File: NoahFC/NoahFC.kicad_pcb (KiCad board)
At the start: 2 copper layers, 40 x 45 mm, 25 parts, among them J1 CH1, J10 GND, J2 CH2, J3 MPU6050, J4 FTDI, J5 8.4V, J6 CH3, J7 PPM, J8 GPS, J9 CH4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

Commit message: revision 1
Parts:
- added J11: SCK, TestPoint:TestPoint_Pad_1.0x1.0mm, F.Cu at (150.8, 88.0)
- added J12: MISO, TestPoint:TestPoint_Pad_1.0x1.0mm, F.Cu at (150.8, 85.4)
- added J13: VCC, TestPoint:TestPoint_Pad_4.0x4.0mm, F.Cu at (159.4, 98.7)
- added J14: GND, TestPoint:TestPoint_Pad_4.0x4.0mm, F.Cu at (154.0, 98.7)
- added R5: 100K, Resistor_SMD:R_0805_2012Metric, F.Cu at (139.4, 90.9)
- added R6: 10K, Resistor_SMD:R_0805_2012Metric, F.Cu at (134.9, 90.9)
- C3: value 100nF -> 1nF
- C5: value 100uF -> 10uF
- D1, D2, D3: footprint LED_SMD:LED_0603_1608Metric -> LED_SMD:LED_0805_2012Metric
- J5: value 8.4V -> VCC
- U1: value ATmega328-A -> ATmega328
- moved C5 36.1 mm to (134.8, 94.1)
- moved J10 34.2 mm to (134.6, 98.7)
- moved C3 34.1 mm to (134.0, 73.2), turned to 180 degrees
- moved J5 29.3 mm to (140.0, 98.7)
- moved R1 23.4 mm to (138.5, 76.9), turned to -90 degrees
- moved C4 22.9 mm to (139.4, 94.1), turned to 0 degrees
- moved U3 21.9 mm to (145.6, 91.0), turned to 90 degrees
- moved J8 18.4 mm to (152.5, 92.7)
- moved J9 17.7 mm to (155.0, 77.5), turned to 90 degrees
- moved J6 14.6 mm to (155.0, 80.1), turned to 90 degrees
- moved D2 13.2 mm to (160.0, 62.2), turned to 0 degrees
- moved R3 13.1 mm to (160.0, 59.3), turned to 0 degrees
- moved J2 11.8 mm to (155.0, 82.7), turned to 90 degrees
- moved D3 11.7 mm to (160.0, 72.4), turned to 0 degrees
- moved D1 11.2 mm to (160.0, 67.3), turned to 0 degrees
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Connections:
- net Net-(C1-Pad1) renamed XTAL1
- net Net-(C2-Pad1) renamed XTAL2
- net Net-(U1-Pad2) renamed LED_MODE
- C3 pad 1: 5V -> RESET
- J1 pad 2: 5V -> 5V_BEC
- J2 pad 2: 5V -> 5V_BEC
- J6 pad 2: unconnected-(J6-Pad2) -> 5V_BEC
- J7 pad 2: 5V -> 5V_BEC
- J9 pad 2: 5V -> 5V_BEC
- R1 pad 1: Net-(R1-Pad1) -> RESET
- R2 pad 1: Net-(U1-Pad32) -> LED_GPS
- R4 pad 1: Net-(U1-Pad9) -> LED_PWR
- U1 pad 11: GPS_RX -> LED_PWR
- U1 pad 16: unconnected-(U1-Pad16) -> MISO
- U1 pad 17: unconnected-(U1-Pad17) -> SCK
- U1 pad 19: unconnected-(U1-Pad19) -> ADC6
- U1 pad 22: unconnected-(U1-Pad22) -> ADC7
- U1 pad 23: unconnected-(U1-Pad23) -> A0
- U1 pad 24: unconnected-(U1-Pad24) -> A1
- U1 pad 25: unconnected-(U1-Pad25) -> VOLTAGE_READ
- U1 pad 26: unconnected-(U1-Pad26) -> A3
- U1 pad 29: Net-(R1-Pad1) -> RESET
- U1 pad 32: Net-(U1-Pad32) -> GPS_RX
- U1 pad 9: Net-(U1-Pad9) -> LED_GPS
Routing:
- net 5V: track 166.3 -> 0.00 mm, vias 10 -> 0
- net GND: track 157.1 -> 0.00 mm
- net DTR: track 44.0 -> 0.00 mm, vias 2 -> 0
- net Net-(U1-Pad32): track 33.9 -> 0.00 mm, vias 2 -> 0
- net Net-(U1-Pad9): track 33.9 -> 0.00 mm, vias 2 -> 0
- net RX: track 24.4 -> 0.00 mm, vias 2 -> 0
- net TX: track 23.9 -> 0.00 mm
- net LED_MODE: track 22.9 -> 0.00 mm, vias 2 -> 0
- net GPS_RX: track 22.8 -> 0.00 mm
- net GPS_TX: track 21.2 -> 0.00 mm
- net SCL: track 19.1 -> 0.00 mm
- net SDA: track 19.0 -> 0.00 mm, vias 2 -> 0
- net PPM: track 18.8 -> 0.00 mm, vias 2 -> 0
- net CH4: track 15.3 -> 0.00 mm, vias 2 -> 0
- net XTAL1: track 14.0 -> 0.00 mm
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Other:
- board size 40 x 45 mm -> 30 x 43 mm
- board text added: "- 8.4v +"
- board text added: "- ESC +"
- board text added: "NoahFC rev1"
- board text added: "http://github.com/zosko/NoahFC by Bosko"
- board text removed: "G"
- board text removed: "NoahFC rev0"
- board text removed: "S"

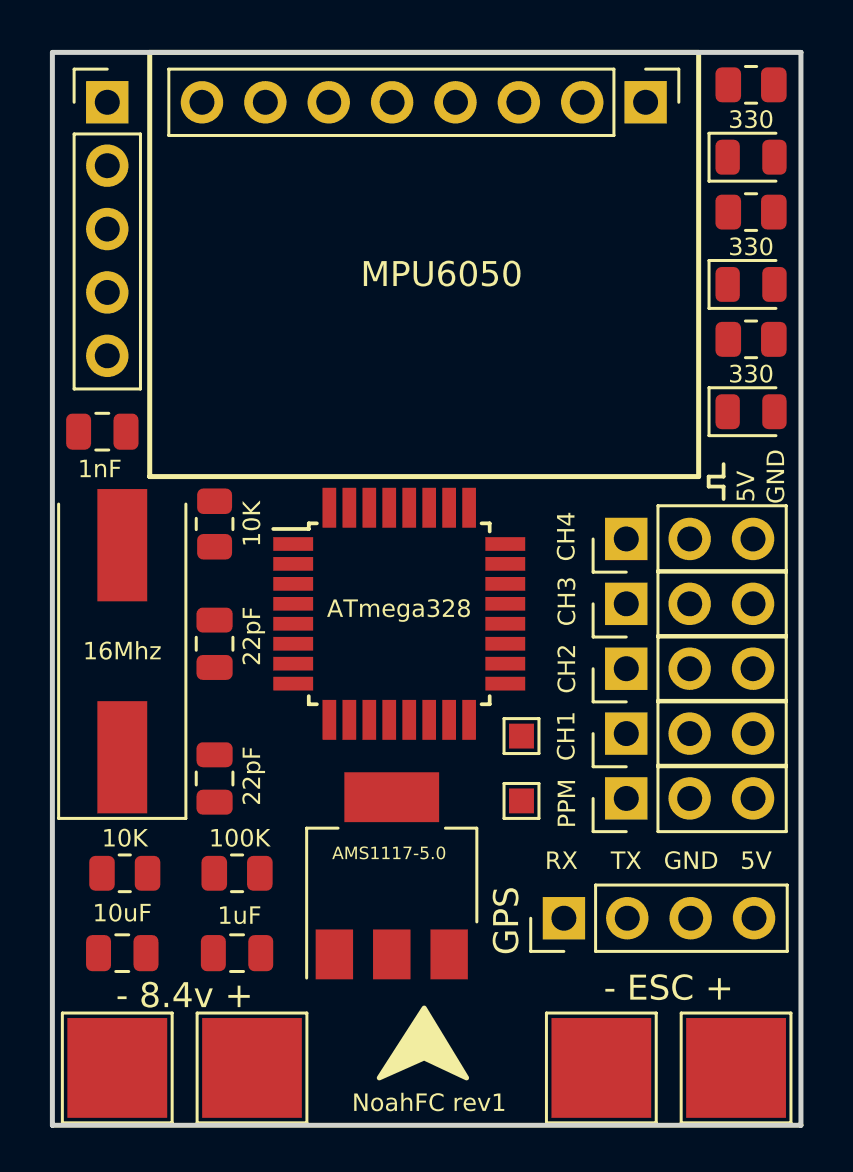
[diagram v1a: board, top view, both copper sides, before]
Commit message: remove one aleron servo
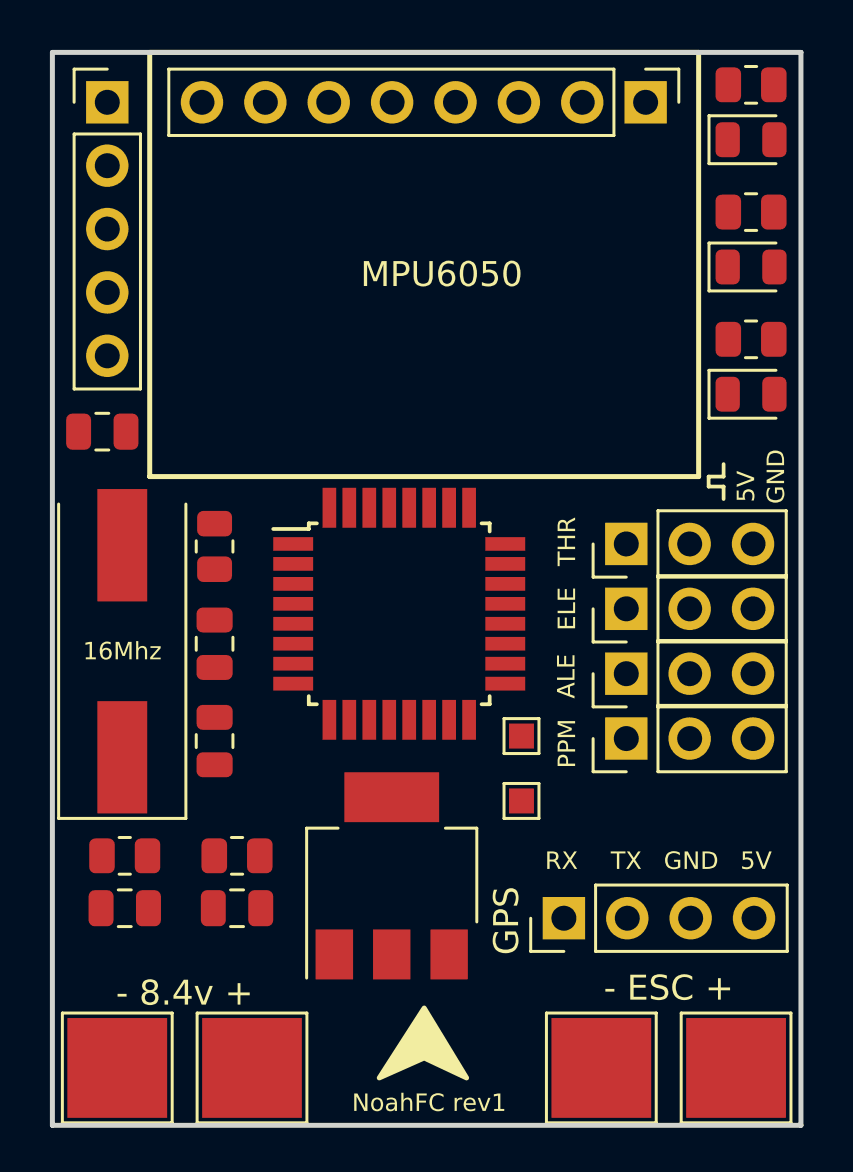
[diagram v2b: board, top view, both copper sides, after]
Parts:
- removed J9: CH4, Connector_PinHeader_2.54mm:PinHeader_1x03_P2.54mm_Vertical
- D1: value PWR -> GPS
- D2: value GPS -> MODE
- D3: value MODE -> PWR
- J1: value CH1 -> ALE
- J2: value CH2 -> ELE
- J6: value CH3 -> THR
- moved J2 2.40 mm to (155.0, 80.3)
- moved J7 2.40 mm to (155.0, 85.5)
- moved J1 2.40 mm to (155.0, 82.9)
- moved J6 2.40 mm to (155.0, 77.7)
- moved C5 1.80 mm to (134.9, 92.3)
- moved C4 1.80 mm to (139.4, 92.3)
- moved C2 1.50 mm to (138.5, 85.6)
- moved R1 0.90 mm to (138.5, 77.8)
- moved D1 0.70 mm to (160.0, 66.6)
- moved D2 0.70 mm to (160.0, 61.5)
- moved D3 0.70 mm to (160.0, 71.7)
- moved R5 0.70 mm to (139.4, 90.2)
- moved R6 0.70 mm to (134.9, 90.2)
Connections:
- net CH1 renamed ALERON
- net CH2 renamed ELEVATOR
- net CH3 renamed THROTTLE
- U1 pad 10: CH4 -> D6

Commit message: route board
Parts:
- added J15: A1, TestPoint:TestPoint_Pad_1.0x1.0mm, F.Cu at (154.5, 76.2)
- added J16: A3, TestPoint:TestPoint_Pad_1.0x1.0mm, F.Cu at (152.4, 76.2)
- added J17: D6, TestPoint:TestPoint_Pad_1.0x1.0mm, F.Cu at (140.9, 87.6)
- added J9: A0, TestPoint:TestPoint_Pad_1.0x1.0mm, F.Cu at (156.7, 76.2)
- moved J2 1.60 mm to (155.0, 81.9)
- moved J1 1.60 mm to (155.0, 84.5)
- moved J6 1.60 mm to (155.0, 79.3)
- moved J7 1.60 mm to (155.0, 87.1)
- moved J12 1.17 mm to (151.4, 86.4)
- moved J11 0.92 mm to (151.4, 88.7)
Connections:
- J1 pad 3: GND -> GND_BEC
- J2 pad 3: GND -> GND_BEC
- J6 pad 3: GND -> GND_BEC
- J7 pad 3: GND -> GND_BEC
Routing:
- net GND: track 0.00 -> 135.7 mm, vias 0 -> 7
- net 5V: track 0.00 -> 120.4 mm, vias 0 -> 7
- net LED_GPS: track 0.00 -> 68.2 mm, vias 0 -> 10
- net VOLTAGE_READ: track 0.00 -> 56.5 mm, vias 0 -> 2
- net LED_MODE: track 0.00 -> 44.0 mm, vias 0 -> 4
- net GPS_RX: track 0.00 -> 41.4 mm, vias 0 -> 1
- net PPM: track 0.00 -> 39.4 mm, vias 0 -> 2
- net VCC: track 0.00 -> 36.0 mm, vias 0 -> 4
- net RESET: track 0.00 -> 27.1 mm, vias 0 -> 2
- net SDA: track 0.00 -> 25.7 mm
- net LED_PWR: track 0.00 -> 23.1 mm, vias 0 -> 2
- net TX: track 0.00 -> 21.4 mm
- net RX: track 0.00 -> 21.0 mm, vias 0 -> 2
- net GPS_TX: track 0.00 -> 20.9 mm, vias 0 -> 1
- net SCL: track 0.00 -> 20.4 mm
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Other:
- board text added: "- VCC +"
- board text removed: "- 8.4v +"

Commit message: rev1 updates
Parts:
- moved J14 5.50 mm to (159.5, 98.6)
- moved J13 4.90 mm to (154.5, 98.6)
- moved J5 0.61 mm to (139.4, 98.6)
- moved J10 0.22 mm to (134.4, 98.6)
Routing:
- net GND: track 135.7 -> 142.8 mm, vias 7 -> 55
- net VCC: track 36.0 -> 32.5 mm, vias 4 -> 2
- net 5V: track 120.4 -> 117.2 mm, vias 7 -> 5
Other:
- board text added: "+ ESC -"
- board text removed: "- ESC +"

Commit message: pin improve
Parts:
- turned R5 to 180 degrees
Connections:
- J7 pad 2: 5V_BEC -> 5V
- J7 pad 3: GND_BEC -> GND
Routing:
- net 5V: track 117.2 -> 124.9 mm
- net GND: track 142.8 -> 150.4 mm
- net VOLTAGE_READ: track 56.5 -> 51.8 mm
- net GND_BEC: track 7.80 -> 5.20 mm
- net 5V_BEC: track 7.80 -> 5.20 mm
- net VCC: track 32.5 -> 31.8 mm

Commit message: fill board
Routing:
- net 5V: track 124.9 -> 127.1 mm
- net PPM: track 39.4 -> 40.9 mm
- net LED_GPS: track 68.2 -> 68.9 mm
- added copper zone on B.Cu, net GND
- added copper zone on F.Cu, net GND

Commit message: add RESET pad
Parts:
- added J18: RESET, TestPoint:TestPoint_Pad_1.0x1.0mm, F.Cu at (138.3, 72.3)
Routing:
- net RESET: track 27.1 -> 29.0 mm
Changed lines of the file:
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@@
       (net 2 "VCC") (pinfunction "Pin_1") (pintype "passive"))
+  )
+  (footprint "TestPoint:TestPoint_Pad_1.0x1.0mm" (layer "F.Cu")
+    (at 138.3 72.3)
+    (descr "SMD rectangular pad as test Point, square 1.0mm side length")
+    (tags "test point SMD pad rectangle square")
+    (property "Sheetfile" "NoahFC.kicad_sch")
+    (property "Sheetname" "")
+    (attr exclude_from_pos_files)
+    (fp_text reference "J18" (at 0 -1.448) (layer "F.SilkS") hide
+      (effects (font (size 1 1) (thickness 0.15)))
+    )
+    (fp_text value "RESET" (at 0 1.55) (layer "F.Fab") hide
+      (effects (font (size 1 1) (thickness 0.15)))
+    )
+    (fp_text user "${REFERENCE}" (at 0 -1.45) (layer "F.Fab") hide
+      (effects (font (size 1 1) (thickness 0.15)))
+    )
+    (fp_line (start -0.7 0.7) (end -0.7 -0.7) (layer "F.SilkS") (width 0.12))
+    (fp_line (start -0.7 -0.7) (end 0.7 -0.7) (layer "F.SilkS") (width 0.12))
+    (fp_line (start 0.7 -0.7) (end 0.7 0.7) (layer "F.SilkS") (width 0.12))
+    (fp_line (start 0.7 0.7) (end -0.7 0.7) (layer "F.SilkS") (width 0.12))
+    (fp_line (start -1 -1) (end 1 -1) (layer "F.CrtYd") (width 0.05))
+    (fp_line (start 1 1) (end -1 1) (layer "F.CrtYd") (width 0.05))
+    (fp_line (start 1 1) (end 1 -1) (layer "F.CrtYd") (width 0.05))
+    (fp_line (start -1 -1) (end -1 1) (layer "F.CrtYd") (width 0.05))
+    (pad "1" smd rect (at 0 0) (size 1 1) (layers "F.Cu" "F.Mask")
+      (net 24 "RESET") (pinfunction "Pin_1") (pintype "passive"))
   )
   (footprint "TestPoint:TestPoint_Pad_4.0x4.0mm" (layer "F.Cu")
@@
   (segment (start 143 75.1) (end 138.5 75.1) (width 0.25) (layer "B.Cu") (net 23))
   (segment (start 138.5 75.1) (end 134.4 79.2) (width 0.25) (layer "B.Cu") (net 23))
+  (segment (start 136.725 71.425) (end 134.95 73.2) (width 0.25) (layer "F.Cu") (net 24))
+  (segment (start 138.3 72.3) (end 137.6 72.3) (width 0.25) (layer "F.Cu") (net 24))
   (segment (start 143.1755 67.3) (end 140.85 67.3) (width 0.25) (layer "F.Cu") (net 24))
+  (segment (start 140.85 67.3) (end 136.725 71.425) (width 0.25) (layer "F.Cu") (net 24))
   (segment (start 145.5 76.25) (end 145.5 67.3) (width 0.25) (layer "F.Cu") (net 24))
+  (segment (start 137.6 72.3) (end 136.725 71.425) (width 0.25) (layer "F.Cu") (net 24))
   (segment (start 134.95 73.3375) (end 138.5 76.8875) (width 0.25) (layer "F.Cu") (net 24))
-  (segment (start 140.85 67.3) (end 134.95 73.2) (width 0.25) (layer "F.Cu") (net 24))
   (segment (start 134.95 73.2) (end 134.95 73.3375) (width 0.25) (layer "F.Cu") (net 24))
   (via (at 145.5 67.3) (size 0.8) (drill 0.4) (layers "F.Cu" "B.Cu") (net 24))

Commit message: add rev2 version board
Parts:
- removed J15: A1, TestPoint:TestPoint_Pad_1.0x1.0mm
- removed J3: MPU6050, Connector_PinHeader_2.54mm:PinHeader_1x08_P2.54mm_Vertical
- removed J9: A0, TestPoint:TestPoint_Pad_1.0x1.0mm
- added C10: 10uF, Capacitor_SMD:C_0805_2012Metric, F.Cu at (143.6, 108.9)
- added C11: 22uF, Capacitor_SMD:C_0805_2012Metric, F.Cu at (139.7, 108.9)
- added C12: 22pF, Capacitor_SMD:C_0805_2012Metric, F.Cu at (120.1, 105.6)
- added C13: 22pF, Capacitor_SMD:C_0805_2012Metric, F.Cu at (120.1, 103.4)
- added C17: 100nF, Capacitor_SMD:C_0805_2012Metric, F.Cu at (140.0, 104.3)
- added C18: 47uF, Capacitor_Tantalum_SMD:CP_EIA-3216-18_Kemet-A, F.Cu at (134.5, 108.8)
- added C19: 47uF, Capacitor_Tantalum_SMD:CP_EIA-3216-18_Kemet-A, F.Cu at (128.8, 108.8)
- added C20: 4.7uF, Capacitor_SMD:C_0805_2012Metric, F.Cu at (144.4, 78.6)
- added C21: 220nF, Capacitor_SMD:C_0805_2012Metric, F.Cu at (142.0, 78.6)
- added C6: 10nF, Capacitor_SMD:C_0805_2012Metric, F.Cu at (126.2, 88.1)
- added C7: 100nF, Capacitor_SMD:C_0805_2012Metric, F.Cu at (128.3, 82.2)
- added C8: 100nF, Capacitor_SMD:C_0805_2012Metric, F.Cu at (123.2, 87.4)
- added C9: 2200pF, Capacitor_SMD:C_0805_2012Metric, F.Cu at (124.4, 76.7)
- added R10: 75, Resistor_SMD:R_0805_2012Metric, F.Cu at (140.0, 102.2)
- added R7: 10K, Resistor_SMD:R_0805_2012Metric, F.Cu at (132.0, 76.8)
- added R8: 10K, Resistor_SMD:R_0805_2012Metric, F.Cu at (132.0, 80.3)
- added R9: 75, Resistor_SMD:R_0805_2012Metric, F.Cu at (140.0, 106.4)
- added U2: MPU-6050, Sensor_Motion:InvenSense_QFN-24_4x4mm_P0.5mm, F.Cu at (122.9, 81.9)
- added U4: AMS1117-3.3, Package_TO_SOT_SMD:SOT-223-3_TabPin2, F.Cu at (141.6, 114.4)
- added U5: MAX7456EUI+, MAX7456:SOP65P637X110-28N, F.Cu at (131.7, 114.9)
- added U6: HMC5883L, HMC5883L:LPCC-16, F.Cu at (137.7, 78.5)
- added Y2: 27Mhz, Crystal:Crystal_SMD_3225-4Pin_3.2x2.5mm, F.Cu at (116.4, 104.5)
- J16: value A3 -> CAM; footprint TestPoint:TestPoint_Pad_1.0x1.0mm -> Connector_PinHeader_2.54mm:PinHeader_1x02_P2.54mm_Vertical
- J17: value D6 -> VTX; footprint TestPoint:TestPoint_Pad_1.0x1.0mm -> Connector_PinHeader_2.54mm:PinHeader_1x02_P2.54mm_Vertical
- Y1: footprint Crystal:Crystal_SMD_HC49-SD -> Crystal:Crystal_SMD_3225-4Pin_3.2x2.5mm
- moved R4 59.9 mm to (133.5, 123.2), turned to 180 degrees
- moved D3 59.6 mm to (130.0, 123.2)
- moved J14 49.4 mm to (116.5, 122.9)
- moved J13 40.9 mm to (121.6, 122.9)
- moved U3 33.0 mm to (122.2, 114.3)
- moved R5 32.3 mm to (130.0, 121.1), turned to 0 degrees
- moved R3 31.2 mm to (131.1, 71.1)
- moved R6 30.9 mm to (133.5, 121.1), turned to 0 degrees
- moved J16 30.1 mm to (147.9, 106.0), turned to -90 degrees
- moved J12 28.8 mm to (129.7, 105.4)
- moved J10 27.5 mm to (147.3, 122.9)
- moved D2 27.2 mm to (134.6, 71.1)
- moved Y1 25.7 mm to (116.4, 100.0)
- moved C1 25.2 mm to (120.1, 98.9), turned to 0 degrees
- moved J11 24.6 mm to (133.4, 105.5)
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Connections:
- J16 pad 1: A3 -> GND
- J17 pad 1: D6 -> GND
- R4 pad 1: LED_PWR -> 5V
- U1 pad 10: D6 -> ELEVATOR
- U1 pad 11: LED_PWR -> LED_GPS
- U1 pad 14: ELEVATOR -> SS
- U1 pad 15: THROTTLE -> MOSI
- U1 pad 19: ADC6 -> unconnected-(U1-Pad19)
- U1 pad 22: ADC7 -> unconnected-(U1-Pad22)
- U1 pad 23: A0 -> unconnected-(U1-Pad23)
- U1 pad 24: A1 -> unconnected-(U1-Pad24)
- U1 pad 26: A3 -> unconnected-(U1-Pad26)
- U1 pad 9: LED_GPS -> THROTTLE
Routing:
- net GND: track 150.2 -> 0.00 mm, vias 55 -> 0
- net 5V: track 127.1 -> 0.00 mm, vias 5 -> 0
- net LED_GPS: track 68.9 -> 0.00 mm, vias 10 -> 0
- net VOLTAGE_READ: track 51.8 -> 0.00 mm, vias 2 -> 0
- net LED_MODE: track 43.8 -> 0.00 mm, vias 4 -> 0
- net GPS_RX: track 41.4 -> 0.00 mm, vias 1 -> 0
- net PPM: track 40.9 -> 0.00 mm, vias 2 -> 0
- net VCC: track 31.8 -> 0.00 mm, vias 2 -> 0
- net RESET: track 29.0 -> 0.00 mm, vias 2 -> 0
- net SDA: track 25.7 -> 0.00 mm
- net LED_PWR: track 23.1 -> 0.00 mm, vias 2 -> 0
- net TX: track 21.4 -> 0.00 mm
- net RX: track 21.0 -> 0.00 mm, vias 2 -> 0
- net GPS_TX: track 20.9 -> 0.00 mm, vias 1 -> 0
- net SCL: track 20.4 -> 0.00 mm
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- removed copper zone on B.Cu, net GND
- removed copper zone on F.Cu, net GND
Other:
- board size 30 x 43 mm -> 36 x 56 mm
- board text removed: "+ ESC -"
- board text removed: "- VCC +"
- board text removed: "NoahFC rev1"
